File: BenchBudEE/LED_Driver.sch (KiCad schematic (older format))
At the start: 6 parts

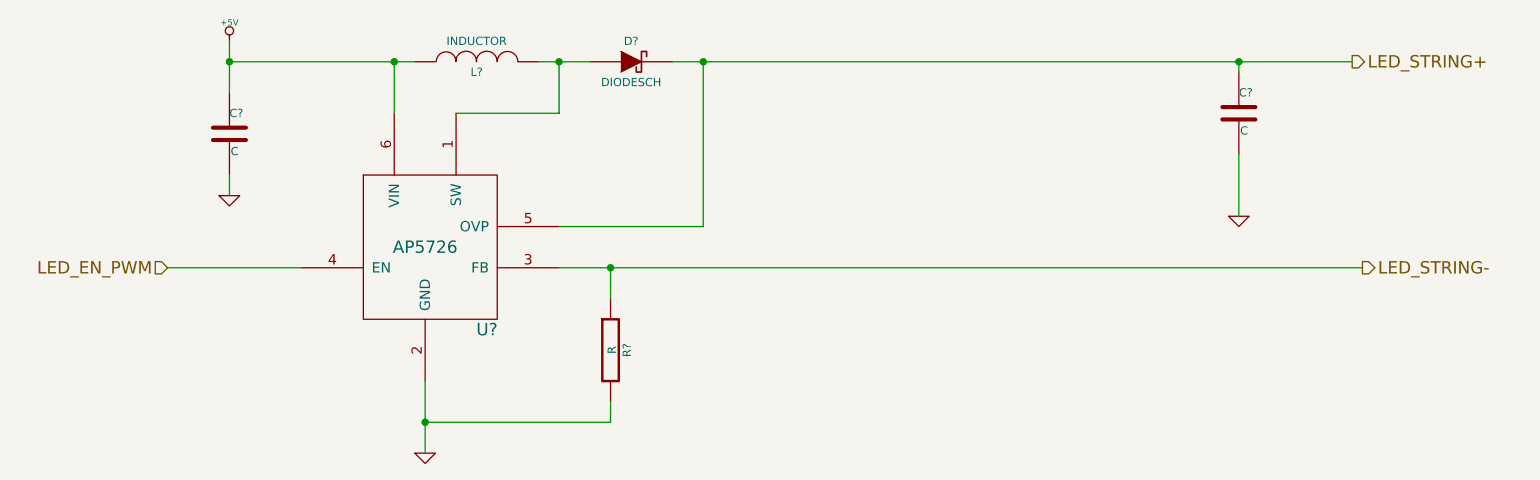
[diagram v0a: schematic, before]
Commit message: Design rules specified for layout.
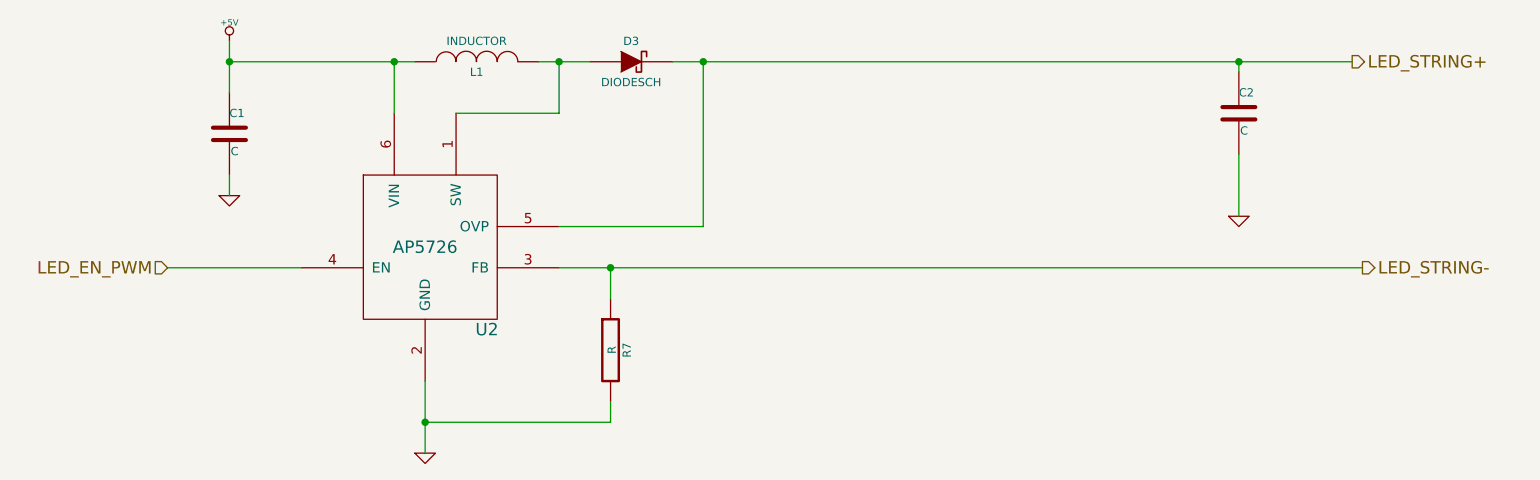
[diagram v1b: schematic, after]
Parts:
- gave numbers to parts that had none: 6
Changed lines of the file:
@@
 LED_STRING-
 $Comp
-L AP5726 U?
+L AP5726 U2
 U 1 1 52F3F91E
 P 5000 2850
-F 0 "U?" H 5300 2450 60  0000 C CNN
+F 0 "U2" H 5300 2450 60  0000 C CNN
 F 1 "AP5726" H 5000 2850 60  0000 C CNN
 F 2 "" H 4950 2900 60  0000 C CNN
@@
 $EndComp
 $Comp
-L +5V #PWR?
+L +5V #PWR3
 U 1 1 52F3FC4A
 P 4050 1850
-F 0 "#PWR?" H 4050 1940 20  0001 C CNN
+F 0 "#PWR3" H 4050 1940 20  0001 C CNN
 F 1 "+5V" H 4050 1940 30  0000 C CNN
 F 2 "" H 4050 1850 60  0000 C CNN
@@
 $EndComp
 $Comp
-L GND #PWR?
+L GND #PWR5
 U 1 1 52F3FC59
 P 5000 3850
-F 0 "#PWR?" H 5000 3850 30  0001 C CNN
+F 0 "#PWR5" H 5000 3850 30  0001 C CNN
 F 1 "GND" H 5000 3780 30  0001 C CNN
 F 2 "" H 5000 3850 60  0000 C CNN
@@
 	5000 3500 5000 3850
 $Comp
-L GND #PWR?
+L GND #PWR4
 U 1 1 52F3FC67
 P 4050 2600
-F 0 "#PWR?" H 4050 2600 30  0001 C CNN
+F 0 "#PWR4" H 4050 2600 30  0001 C CNN
 F 1 "GND" H 4050 2530 30  0001 C CNN
 F 2 "" H 4050 2600 60  0000 C CNN
@@
 $EndComp
 $Comp
-L C C?
+L C C1
 U 1 1 52F3FC6F
 P 4050 2300
-F 0 "C?" H 4050 2400 40  0000 L CNN
+F 0 "C1" H 4050 2400 40  0000 L CNN
 F 1 "C" H 4056 2215 40  0000 L CNN
 F 2 "~" H 4088 2150 30  0000 C CNN
@@
 Connection ~ 4050 1950
 $Comp
-L INDUCTOR L?
+L INDUCTOR L1
 U 1 1 52F3FC91
 P 5250 1950
-F 0 "L?" V 5200 1950 40  0000 C CNN
+F 0 "L1" V 5200 1950 40  0000 C CNN
 F 1 "INDUCTOR" V 5350 1950 40  0000 C CNN
 F 2 "~" H 5250 1950 60  0000 C CNN
@@
 	5650 2200 5150 2200
 $Comp
-L DIODESCH D?
+L DIODESCH D3
 U 1 1 52F3FCBF
 P 6000 1950
-F 0 "D?" H 6000 2050 40  0000 C CNN
+F 0 "D3" H 6000 2050 40  0000 C CNN
 F 1 "DIODESCH" H 6000 1850 40  0000 C CNN
 F 2 "~" H 6000 1950 60  0000 C CNN
@@
 	6200 1950 9500 1950
 $Comp
-L C C?
+L C C2
 U 1 1 52F3FCE4
 P 8950 2200
-F 0 "C?" H 8950 2300 40  0000 L CNN
+F 0 "C2" H 8950 2300 40  0000 L CNN
 F 1 "C" H 8956 2115 40  0000 L CNN
 F 2 "~" H 8988 2050 30  0000 C CNN
@@
 Connection ~ 6350 1950
 $Comp
-L GND #PWR?
+L GND #PWR6
 U 1 1 52F3FCF9
 P 8950 2700
-F 0 "#PWR?" H 8950 2700 30  0001 C CNN
+F 0 "#PWR6" H 8950 2700 30  0001 C CNN
 F 1 "GND" H 8950 2630 30  0001 C CNN
 F 2 "" H 8950 2700 60  0000 C CNN
@@
 	9550 2950 5650 2950
 $Comp
-L R R?
+L R R7
 U 1 1 52F3FD3D
 P 5900 3350
-F 0 "R?" V 5980 3350 40  0000 C CNN
+F 0 "R7" V 5980 3350 40  0000 C CNN
 F 1 "R" V 5907 3351 40  0000 C CNN
 F 2 "~" V 5830 3350 30  0000 C CNN

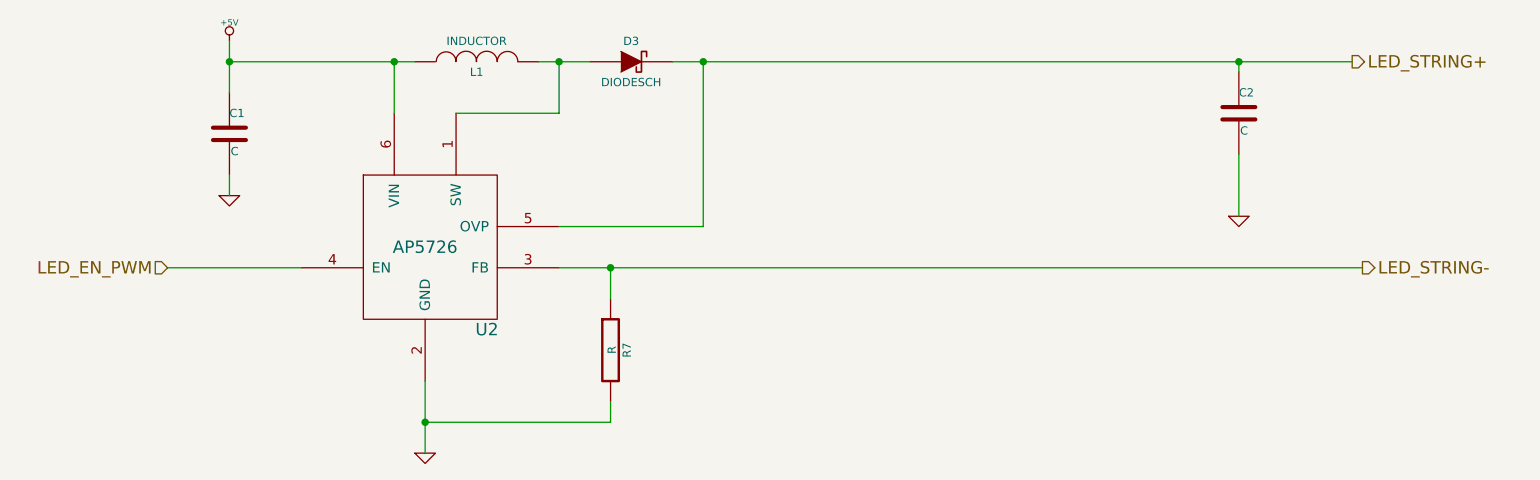
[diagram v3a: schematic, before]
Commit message: All modules (inc. LED Driver) associated + roughly placed.
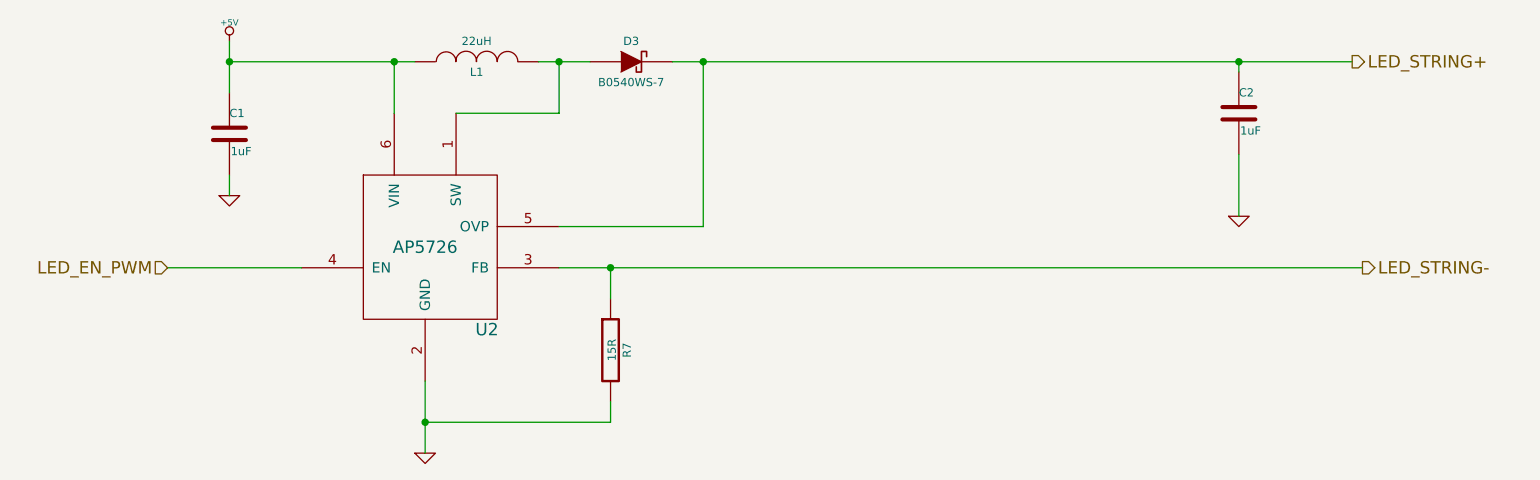
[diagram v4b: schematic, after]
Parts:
- C1, C2: value C -> 1uF
- D3: value DIODESCH -> B0540WS-7; Distributor (none) -> DigiKey; Distributor Part Link (none) -> http://www.digikey.com/product-detail/en/B0540WS-7/B0540WSD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; Distributor Part Number (none) -> B0540WSDICT-ND; MFG Name (none) -> Diodes Incorporated; MFG Part Number (none) -> B0540WS-7
- L1: value INDUCTOR -> 22uH; Distributor (none) -> DigiKey; Distributor Part Link (none) -> http://www.digikey.com/product-detail/en/NR4012T220M/587-16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; Distributor Part Number (none) -> 587-1660-1-ND; MFG Name (none) -> Taiyo Yuden; MFG Part Number (none) -> NR4012T220M
- R7: value R -> 15R
- U2: Distributor (none) -> DigiKey; Distributor Part Link (none) -> http://www.digikey.com/product-detail/en/AP5726WG-7/AP5726W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; Distributor Part Number (none) -> AP5726WG-7DICT-ND; MFG Name (none) -> Diodes Incorporated; MFG Part Number (none) -> AP5726WG-7
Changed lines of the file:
@@
 Sheet 3 9
 Title ""
-Date "23 feb 2014"
+Date "24 feb 2014"
 Rev ""
 Comp ""
@@
 F 1 "AP5726" H 5000 2850 60  0000 C CNN
 F 2 "" H 4950 2900 60  0000 C CNN
-F 3 "" H 4950 2900 60  0000 C CNN
+F 3 "http://www.diodes.com/datasheets/AP5726.pdf" H 4950 2900 60  0001 C CNN
+F 4 "Diodes Incorporated" H 5000 2850 60  0001 C CNN "MFG Name"
+F 5 "AP5726WG-7" H 5000 2850 60  0001 C CNN "MFG Part Number"
+F 6 "DigiKey" H 5000 2850 60  0001 C CNN "Distributor"
+F 7 "AP5726WG-7DICT-ND" H 5000 2850 60  0001 C CNN "Distributor Part Number"
+F 8 "http://www.digikey.com/product-detail/en/AP5726WG-7/AP5726WG-7DICT-ND/2639342" H 5000 2850 60  0001 C CNN "Distributor Part Link"
 	1    5000 2850
 	1    0    0    -1
@@
 P 4050 2300
 F 0 "C1" H 4050 2400 40  0000 L CNN
-F 1 "C" H 4056 2215 40  0000 L CNN
+F 1 "1uF" H 4056 2215 40  0000 L CNN
 F 2 "~" H 4088 2150 30  0000 C CNN
 F 3 "~" H 4050 2300 60  0000 C CNN
@@
 P 5250 1950
 F 0 "L1" V 5200 1950 40  0000 C CNN
-F 1 "INDUCTOR" V 5350 1950 40  0000 C CNN
+F 1 "22uH" V 5350 1950 40  0000 C CNN
 F 2 "~" H 5250 1950 60  0000 C CNN
-F 3 "~" H 5250 1950 60  0000 C CNN
+F 3 "http://www.yuden.co.jp/ut/product/category/inductor/NR4012T220M.pdf" H 5250 1950 60  0001 C CNN
+F 4 "Taiyo Yuden" H 5250 1950 60  0001 C CNN "MFG Name"
+F 5 "NR4012T220M" H 5250 1950 60  0001 C CNN "MFG Part Number"
+F 6 "DigiKey" H 5250 1950 60  0001 C CNN "Distributor"
+F 7 "587-1660-1-ND" H 5250 1950 60  0001 C CNN "Distributor Part Number"
+F 8 "http://www.digikey.com/product-detail/en/NR4012T220M/587-1660-1-ND/1008275" H 5250 1950 60  0001 C CNN "Distributor Part Link"
 	1    5250 1950
 	0    -1   -1   0
@@
 P 6000 1950
 F 0 "D3" H 6000 2050 40  0000 C CNN
-F 1 "DIODESCH" H 6000 1850 40  0000 C CNN
+F 1 "B0540WS-7" H 6000 1850 40  0000 C CNN
 F 2 "~" H 6000 1950 60  0000 C CNN
-F 3 "~" H 6000 1950 60  0000 C CNN
+F 3 "http://www.diodes.com/datasheets/ds30524.pdf" H 6000 1950 60  0001 C CNN
+F 4 "Diodes Incorporated" H 6000 1950 60  0001 C CNN "MFG Name"
+F 5 "B0540WS-7" H 6000 1950 60  0001 C CNN "MFG Part Number"
+F 6 "DigiKey" H 6000 1950 60  0001 C CNN "Distributor"
+F 7 "B0540WSDICT-ND" H 6000 1950 60  0001 C CNN "Distributor Part Number"
+F 8 "http://www.digikey.com/product-detail/en/B0540WS-7/B0540WSDICT-ND/816549" H 6000 1950 60  0001 C CNN "Distributor Part Link"
 	1    6000 1950
 	1    0    0    -1
@@
 P 8950 2200
 F 0 "C2" H 8950 2300 40  0000 L CNN
-F 1 "C" H 8956 2115 40  0000 L CNN
+F 1 "1uF" H 8956 2115 40  0000 L CNN
 F 2 "~" H 8988 2050 30  0000 C CNN
 F 3 "~" H 8950 2200 60  0000 C CNN
@@
 P 5900 3350
 F 0 "R7" V 5980 3350 40  0000 C CNN
-F 1 "R" V 5907 3351 40  0000 C CNN
+F 1 "15R" V 5907 3351 40  0000 C CNN
 F 2 "~" V 5830 3350 30  0000 C CNN
 F 3 "~" H 5900 3350 30  0000 C CNN
